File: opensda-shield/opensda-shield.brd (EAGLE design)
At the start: 21.6 x 53.3 mm, 17 parts, among them IC1 74LVC125, IC2 74LVC125, J1 61302011121, J2 61302011121, J3 61300211121, J4 CORTEX_DEBUG_PTH, J5 61301511121

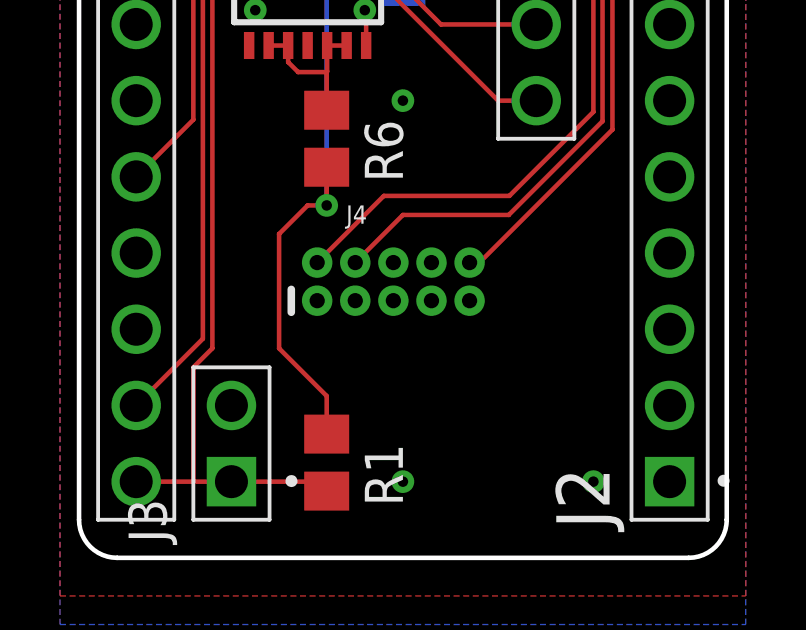
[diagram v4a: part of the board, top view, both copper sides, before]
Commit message: Male presuny
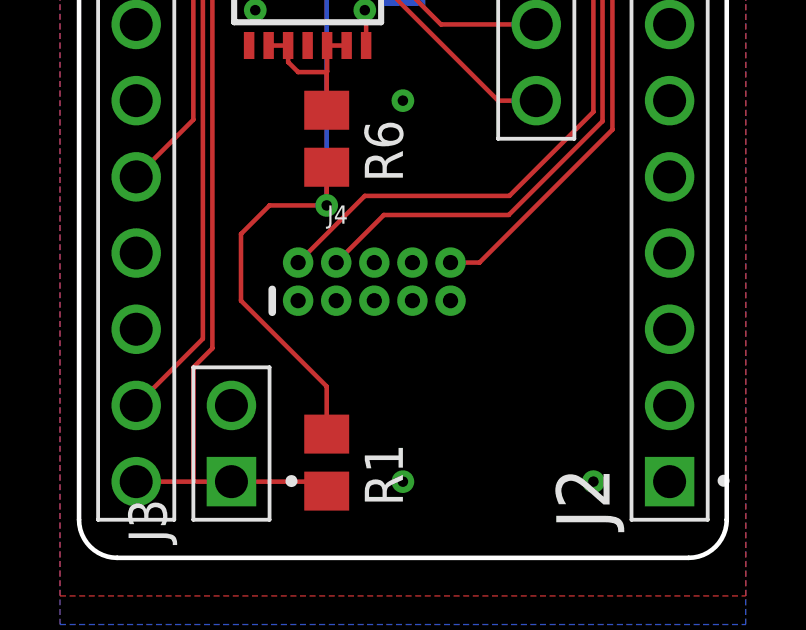
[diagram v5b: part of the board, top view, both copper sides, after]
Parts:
- moved J4 0.63 mm to (9.84, 9.21)
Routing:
- net 3V3: track 79.4 -> 81.2 mm
- net SWD_CLK_TGT: track 32.8 -> 33.5 mm
- net !RST_TGT: track 36.7 -> 37.3 mm
- net SWD_DIO_TGT: track 51.7 -> 52.4 mm
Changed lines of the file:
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@@
 <circle x="18.415" y="1.5875" radius="0.0762" width="0.3048" layer="111"/>
 <text x="8.89" y="5.3975" size="1.143" layer="111" ratio="15" align="bottom-center">BOOT</text>
-<text x="6.0325" y="7.9375" size="1.143" layer="111">1</text>
-<text x="13.97" y="1.5875" size="1.27" layer="111" align="bottom-center">OpenSDA
+<text x="5.3975" y="7.9375" size="1.143" layer="111">1</text>
+<text x="13.6525" y="1.27" size="1.397" layer="111" align="bottom-center">OpenSDA
 shield</text>
 </plain>
@@
 <attribute name="VALUE" x="8.763" y="0.508" size="1.27" layer="27" rot="R90"/>
 </element>
-<element name="J4" library="SparkFun-Connectors" library_urn="urn:adsk.eagle:library:513" package="2X5-PTH-1.27MM" package3d_urn="urn:adsk.eagle:package:38290/1" value="CORTEX_DEBUG_PTH" x="10.4775" y="9.2075" smashed="yes">
-<attribute name="NAME" x="8.9027" y="11.1379" size="0.6096" layer="25" font="vector" ratio="20"/>
-<attribute name="VALUE" x="8.6487" y="6.7437" size="0.6096" layer="27" font="vector" ratio="20"/>
+<element name="J4" library="SparkFun-Connectors" library_urn="urn:adsk.eagle:library:513" package="2X5-PTH-1.27MM" package3d_urn="urn:adsk.eagle:package:38290/1" value="CORTEX_DEBUG_PTH" x="9.8425" y="9.2075" smashed="yes">
+<attribute name="NAME" x="8.2677" y="11.1379" size="0.6096" layer="25" font="vector" ratio="20"/>
+<attribute name="VALUE" x="8.0137" y="6.7437" size="0.6096" layer="27" font="vector" ratio="20"/>
 </element>
 <element name="J5" library="Headers" library_urn="urn:adsk.eagle:library:11687645" package="61301511121" package3d_urn="urn:adsk.eagle:package:11391913/2" value="61301511121" x="15.24" y="33.02" smashed="yes" rot="R270">
@@
 <via x="8.255" y="11.7475" extent="1-16" drill="0.35"/>
 <wire x1="8.255" y1="11.7475" x2="8.255" y2="19.05" width="0.1524" layer="16"/>
-<wire x1="7.62" y1="11.7475" x2="8.255" y2="11.7475" width="0.1524" layer="1"/>
-<wire x1="7.62" y1="11.7475" x2="6.6675" y2="10.795" width="0.1524" layer="1"/>
-<wire x1="6.6675" y1="10.795" x2="6.6675" y2="6.9825" width="0.1524" layer="1"/>
-<wire x1="8.255" y1="4.125" x2="8.255" y2="5.395" width="0.1524" layer="1"/>
-<wire x1="8.255" y1="5.395" x2="6.6675" y2="6.9825" width="0.1524" layer="1"/>
+<wire x1="6.35" y1="11.7475" x2="8.255" y2="11.7475" width="0.1524" layer="1"/>
+<wire x1="6.35" y1="11.7475" x2="5.3975" y2="10.795" width="0.1524" layer="1"/>
+<wire x1="5.3975" y1="10.795" x2="5.3975" y2="8.57" width="0.1524" layer="1"/>
+<wire x1="8.255" y1="4.125" x2="8.255" y2="5.7125" width="0.1524" layer="1"/>
+<wire x1="8.255" y1="5.7125" x2="5.3975" y2="8.57" width="0.1524" layer="1"/>
 <wire x1="1.905" y1="43.18" x2="3.81" y2="43.18" width="0.3048" layer="1"/>
 <wire x1="3.81" y1="43.18" x2="6.0325" y2="40.9575" width="0.3048" layer="1"/>
@@
 <wire x1="15.24" y1="22.86" x2="13.6525" y2="24.4475" width="0.1524" layer="16"/>
 <wire x1="17.145" y1="14.86535" x2="14.34465" y2="12.065" width="0.1524" layer="1"/>
-<wire x1="7.9375" y1="9.8425" x2="10.16" y2="12.065" width="0.1524" layer="1"/>
-<wire x1="14.34465" y1="12.065" x2="10.16" y2="12.065" width="0.1524" layer="1"/>
+<wire x1="7.3025" y1="9.8425" x2="9.525" y2="12.065" width="0.1524" layer="1"/>
+<wire x1="14.34465" y1="12.065" x2="9.525" y2="12.065" width="0.1524" layer="1"/>
 <wire x1="17.145" y1="20.955" x2="15.24" y2="22.86" width="0.1524" layer="1"/>
 <wire x1="17.145" y1="14.86535" x2="17.145" y2="20.955" width="0.1524" layer="1"/>
@@
 <wire x1="7.62" y1="32" x2="7.62" y2="31.115" width="0.1524" layer="1"/>
 <wire x1="17.4498" y1="21.9202" x2="17.4498" y2="14.5542" width="0.1524" layer="1"/>
-<wire x1="14.3256" y1="11.43" x2="10.795" y2="11.43" width="0.1524" layer="1"/>
-<wire x1="9.2075" y1="9.8425" x2="10.795" y2="11.43" width="0.1524" layer="1"/>
+<wire x1="14.3256" y1="11.43" x2="10.16" y2="11.43" width="0.1524" layer="1"/>
+<wire x1="8.5725" y1="9.8425" x2="10.16" y2="11.43" width="0.1524" layer="1"/>
 <wire x1="17.4498" y1="14.5542" x2="14.3256" y2="11.43" width="0.1524" layer="1"/>
 <wire x1="15.24" y1="25.4" x2="17.145" y2="23.495" width="0.1524" layer="16"/>
@@
 <contactref element="J4" pad="10"/>
 <contactref element="IC1" pad="8"/>
-<wire x1="13.0175" y1="9.8425" x2="13.3477" y2="9.8425" width="0.1524" layer="1"/>
+<wire x1="12.3825" y1="9.8425" x2="13.3477" y2="9.8425" width="0.1524" layer="1"/>
 <wire x1="18.06575" y1="21.3487" x2="17.78" y2="21.06295" width="0.1524" layer="1"/>
 <wire x1="17.78" y1="21.06295" x2="17.78" y2="14.2748" width="0.1524" layer="1"/>

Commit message: OpenSDA shield v1.1
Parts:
- moved R1 0.32 mm to (7.94, 3.17)
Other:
- board text added: "JV & poli 2022"
- board text added: "OpenSDA shield v1.1"
- board text removed: "OpenSDA shield"
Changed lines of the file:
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@@
 <circle x="3.81" y="51.7525" radius="0.0762" width="0.3048" layer="111"/>
 <circle x="13.97" y="51.7525" radius="0.0762" width="0.3048" layer="111"/>
-<circle x="18.415" y="1.5875" radius="0.0762" width="0.3048" layer="111"/>
+<circle x="18.415" y="0.635" radius="0.0762" width="0.3048" layer="111"/>
 <text x="8.89" y="5.3975" size="1.143" layer="111" ratio="15" align="bottom-center">BOOT</text>
 <text x="5.3975" y="7.9375" size="1.143" layer="111">1</text>
-<text x="13.6525" y="1.27" size="1.397" layer="111" align="bottom-center">OpenSDA
-shield</text>
+<text x="13.6525" y="1.27" size="1.27" layer="111" align="bottom-center">OpenSDA
+shield v1.1</text>
+<text x="17.78" y="1.27" size="1.143" layer="16" rot="MR0">JV &amp; poli 2022</text>
+<text x="17.78" y="1.27" size="1.143" layer="40" rot="MR0">JV &amp; poli 2022</text>
 </plain>
 <attributes>
@@
 <attribute name="VALUE" x="9.525" y="48.26" size="1.27" layer="27" rot="R90"/>
 </element>
-<element name="R1" library="rcl" library_urn="urn:adsk.eagle:library:334" package="R0805" package3d_urn="urn:adsk.eagle:package:23553/2" value="10k" x="8.255" y="3.175" smashed="yes" rot="R270">
-<attribute name="NAME" x="9.525" y="3.81" size="1.27" layer="25" rot="R270"/>
-<attribute name="POPULARITY" value="86" x="-34.925" y="-32.385" size="1.778" layer="27" rot="R270" display="off"/>
-<attribute name="SPICEPREFIX" value="R" x="-34.925" y="-32.385" size="1.778" layer="27" rot="R270" display="off"/>
-<attribute name="VALUE" x="5.715" y="3.81" size="1.27" layer="27" rot="R270"/>
+<element name="R1" library="rcl" library_urn="urn:adsk.eagle:library:334" package="R0805" package3d_urn="urn:adsk.eagle:package:23553/2" value="10k" x="7.9375" y="3.175" smashed="yes" rot="R270">
+<attribute name="NAME" x="9.2075" y="3.81" size="1.27" layer="25" rot="R270"/>
+<attribute name="POPULARITY" value="86" x="-35.2425" y="-32.385" size="1.778" layer="27" rot="R270" display="off"/>
+<attribute name="SPICEPREFIX" value="R" x="-35.2425" y="-32.385" size="1.778" layer="27" rot="R270" display="off"/>
+<attribute name="VALUE" x="5.3975" y="3.81" size="1.27" layer="27" rot="R270"/>
 </element>
 <element name="R2" library="rcl" library_urn="urn:adsk.eagle:library:334" package="R0805" package3d_urn="urn:adsk.eagle:package:23553/2" value="10k" x="5.08" y="27.305" smashed="yes" rot="R270">
@@
 <via x="5.87375" y="21.59" extent="1-16" drill="0.35"/>
 <via x="10.795" y="15.24" extent="1-16" drill="0.35"/>
-<via x="10.795" y="2.54" extent="1-16" drill="0.35"/>
-<via x="17.145" y="2.54" extent="1-16" drill="0.35"/>
+<via x="11.7475" y="6.0325" extent="1-16" drill="0.35"/>
+<via x="16.8275" y="6.0325" extent="1-16" drill="0.35"/>
 <via x="17.4625" y="31.4325" extent="1-16" drill="0.35"/>
 <via x="5.87375" y="18.25625" extent="1-16" drill="0.35"/>
@@
 <wire x1="6.35" y1="11.7475" x2="5.3975" y2="10.795" width="0.1524" layer="1"/>
 <wire x1="5.3975" y1="10.795" x2="5.3975" y2="8.57" width="0.1524" layer="1"/>
-<wire x1="8.255" y1="4.125" x2="8.255" y2="5.7125" width="0.1524" layer="1"/>
-<wire x1="8.255" y1="5.7125" x2="5.3975" y2="8.57" width="0.1524" layer="1"/>
+<wire x1="7.9375" y1="4.125" x2="7.9375" y2="6.03" width="0.1524" layer="1"/>
+<wire x1="7.9375" y1="6.03" x2="5.3975" y2="8.57" width="0.1524" layer="1"/>
 <wire x1="1.905" y1="43.18" x2="3.81" y2="43.18" width="0.3048" layer="1"/>
 <wire x1="3.81" y1="43.18" x2="6.0325" y2="40.9575" width="0.3048" layer="1"/>
@@
 <contactref element="J3" pad="1"/>
 <contactref element="IC1" pad="10"/>
-<wire x1="8.255" y1="2.225" x2="7.94" y2="2.54" width="0.1524" layer="1"/>
-<wire x1="5.08" y1="2.54" x2="7.94" y2="2.54" width="0.1524" layer="1"/>
+<wire x1="7.9375" y1="2.225" x2="7.6225" y2="2.54" width="0.1524" layer="1"/>
+<wire x1="5.08" y1="2.54" x2="7.6225" y2="2.54" width="0.1524" layer="1"/>
 <wire x1="1.905" y1="2.54" x2="3.81" y2="2.54" width="0.1524" layer="1"/>
 <wire x1="3.81" y1="2.54" x2="5.08" y2="2.54" width="0.1524" layer="1"/>
